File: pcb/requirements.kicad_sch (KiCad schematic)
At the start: 0 parts

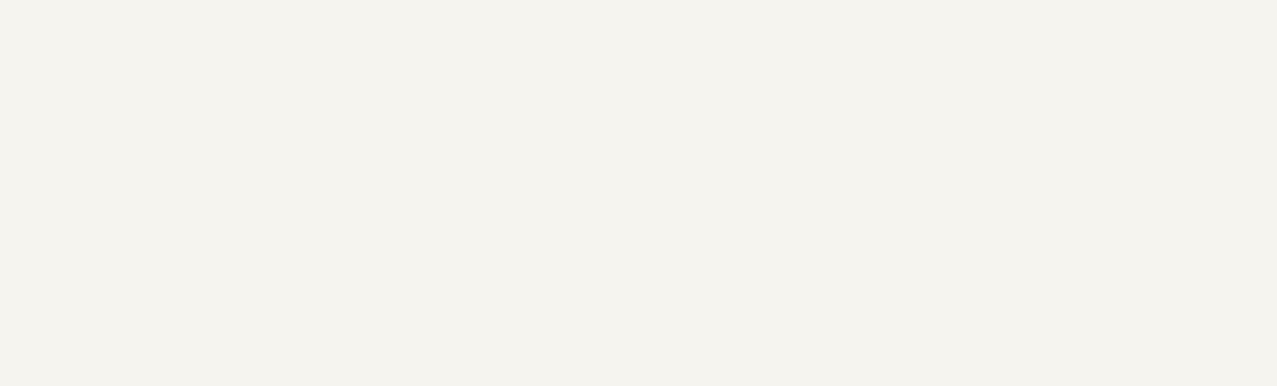
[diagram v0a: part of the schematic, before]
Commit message: Added second power connector
Rearranged.
Added additional filtering
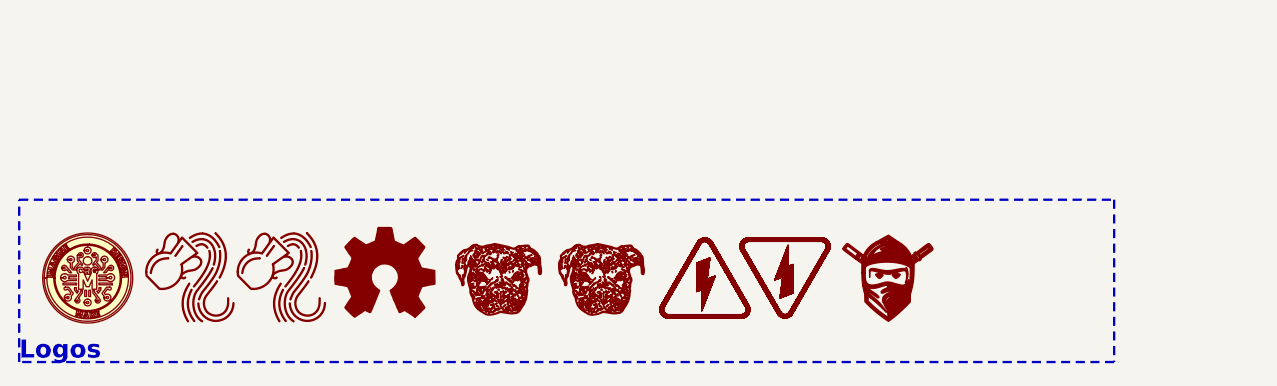
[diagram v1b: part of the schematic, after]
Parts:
- added LOGO1: ~, CRGM Logos:CRGM Logo 10mm, symbol CRGM Logos:CRGM Logo
- added LOGO2: ~, Symbol:OSHW-Logo_5.7x6mm_SilkScreen, symbol Graphic:Logo_Open_Hardware_Small
- added LOGO3: ~, CRGM Logos:Aquarius Logo 10mm, symbol CRGM Logos:Aquarius Logo
- added LOGO4: ~, CRGM Logos:Aquarius Logo 5mm, symbol CRGM Logos:Aquarius Logo
- added LOGO5: ~, CRGM Logos:Roxy 8mm, symbol CRGM Logos:Roxy Logo
- added LOGO6: ~, CRGM Logos:FNWW Face 5mm, symbol CRGM Logos:FNWW Face
- added LOGO7: ~, CRGM Logos:Roxy 5mm, symbol CRGM Logos:Roxy Logo
- added S1, S2: ~, CRGM Symbols:HIGH-VOLTAGE-5MM, symbol CRGM Symbols:High Voltage
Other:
- note added: "Logos"
